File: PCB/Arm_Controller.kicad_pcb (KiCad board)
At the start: 2 copper layers, 156 parts, among them J1 CAN SOCKET, J11 BTN1, J12 FAN1, J15 SWD Header, J2 EXTERNAL POWER, J3 BATTERY POWER, J4 STEP_MOTOR_1, J5 STEP_MOTOR_2, J6 STEP_MOTOR_3, J7 STEP_MOTOR_4, J8 STEP_MOTOR_5, J9 STEP_MOTOR_6, U1 STM32G431CBT6, U10 TMC2209-LA-T, U11 TMC2209-LA-T, U2 XL4005E1, U3 NCP1117-3.3_SOT223, U5 TMC2209-LA-T, U6 ISO1042DWVR, U7 TMC2209-LA-T, U8 TMC2209-LA-T, U9 TMC2209-LA-T, Y1 8MHz

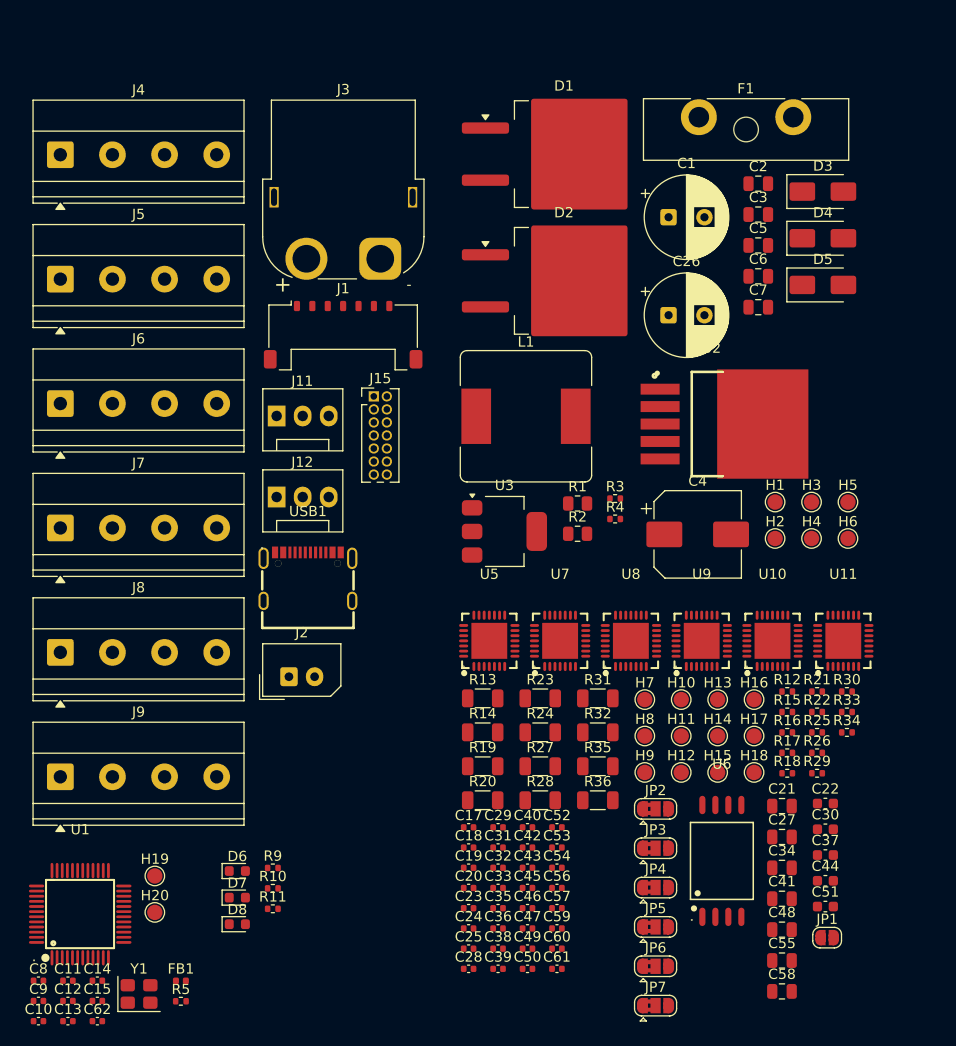
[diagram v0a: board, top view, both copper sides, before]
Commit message: Improved Protection and Board Testability - Added power rail protection and decoupling for stepper motor noise environment - Added TVS, bulk caps and fuse upgrade on 24V rail - Added test pads for bring-up and debugging
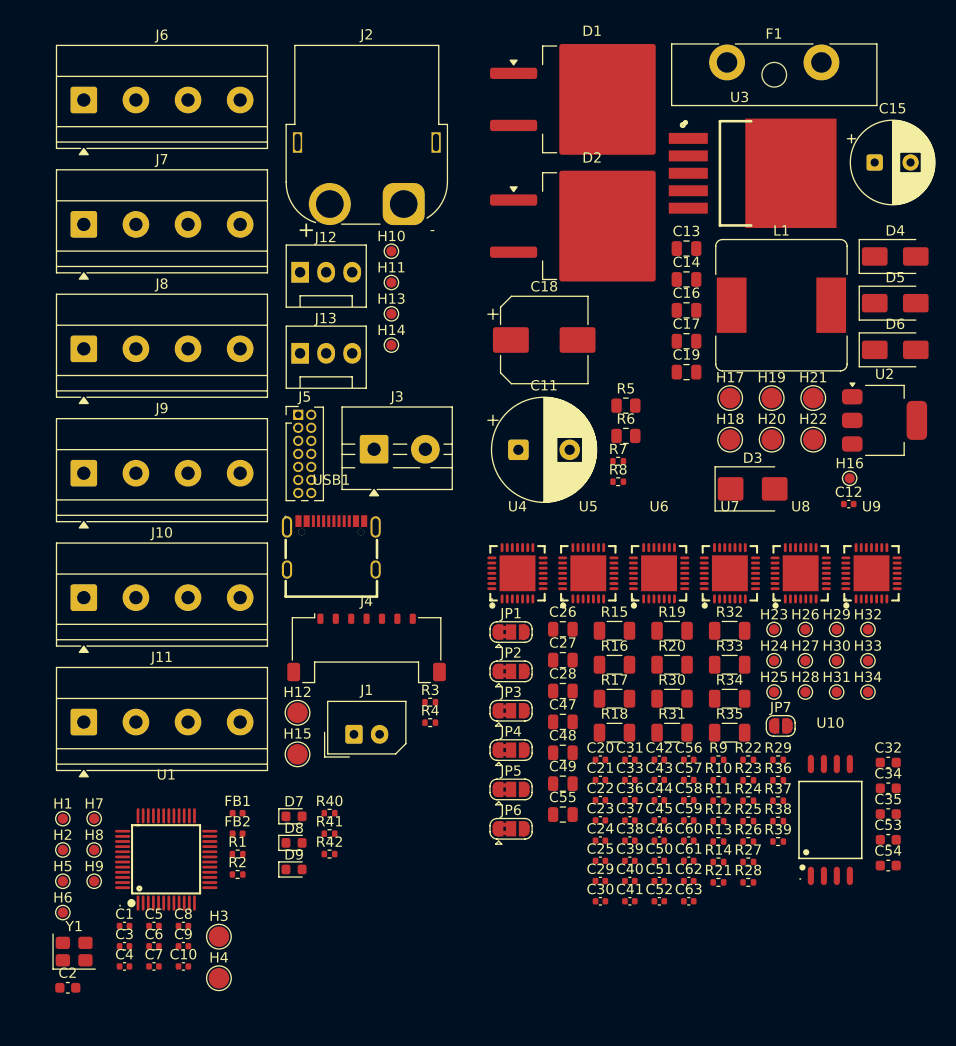
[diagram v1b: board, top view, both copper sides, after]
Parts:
- removed J15: SWD Header, Connector_PinHeader_1.27mm:PinHeader_2x07_P1.27mm_Vertical
- removed U11: TMC2209-LA-T, lcsc:QFN-28_L5.0-W5.0-P0.50-BL-EP
- added C16: 1uF, Capacitor_SMD:C_0805_2012Metric, F.Cu at (139.5, 76.8)
- added C63: 100nF, Capacitor_SMD:C_0402_1005Metric, F.Cu at (139.7, 134.4)
- added D9: LED_GREEN, LED_SMD:LED_0603_1608Metric, F.Cu at (101.3, 131.3)
- added FB2: 1kR@100MHz, Inductor_SMD:L_0402_1005Metric, F.Cu at (95.8, 127.8)
- added H21: +24V, TestPoint:TestPoint_Pad_D2.0mm, F.Cu at (151.9, 85.3)
- added H22: +VBUS, TestPoint:TestPoint_Pad_D2.0mm, F.Cu at (151.9, 89.4)
- added H23: TMC1_DIAG, TestPoint:TestPoint_Pad_D1.0mm, F.Cu at (148.1, 107.9)
- added H24: TMC2_DIAG, TestPoint:TestPoint_Pad_D1.0mm, F.Cu at (148.1, 110.9)
- added H25: TMC3_DIAG, TestPoint:TestPoint_Pad_D1.0mm, F.Cu at (148.1, 114.0)
- added H26: TMC1_INDEX, TestPoint:TestPoint_Pad_D1.0mm, F.Cu at (151.1, 107.9)
- added H27: TMC2_INDEX, TestPoint:TestPoint_Pad_D1.0mm, F.Cu at (151.1, 110.9)
- added H28: TMC3_INDEX, TestPoint:TestPoint_Pad_D1.0mm, F.Cu at (151.1, 114.0)
- added H29: TMC4_DIAG, TestPoint:TestPoint_Pad_D1.0mm, F.Cu at (154.2, 107.9)
- added H30: TMC5_DIAG, TestPoint:TestPoint_Pad_D1.0mm, F.Cu at (154.2, 110.9)
- added H31: TMC6_DIAG, TestPoint:TestPoint_Pad_D1.0mm, F.Cu at (154.2, 114.0)
- added H32: TMC4_INDEX, TestPoint:TestPoint_Pad_D1.0mm, F.Cu at (157.2, 107.9)
- added H33: TMC5_INDEX, TestPoint:TestPoint_Pad_D1.0mm, F.Cu at (157.2, 110.9)
- added H34: TMC6_INDEX, TestPoint:TestPoint_Pad_D1.0mm, F.Cu at (157.2, 114.0)
- added J10: STEP_MOTOR_5, TerminalBlock_Phoenix:TerminalBlock_Phoenix_MKDS-1,5-4-5.08_1x04_P5.08mm_Horizontal, F.Cu at (80.8, 104.8)
- added J13: FAN1, Connector:FanPinHeader_1x03_P2.54mm_Vertical, F.Cu at (101.9, 81.0)
- added R37: 20kR, Resistor_SMD:R_0402_1005Metric, F.Cu at (148.5, 124.6)
- added R38: 20kR, Resistor_SMD:R_0402_1005Metric, F.Cu at (148.5, 126.6)
- added R39: 120R, Resistor_SMD:R_0402_1005Metric, F.Cu at (148.5, 128.6)
- added R40: 1.1kR, Resistor_SMD:R_0402_1005Metric, F.Cu at (104.7, 125.8)
- added R41: 1kR, Resistor_SMD:R_0402_1005Metric, F.Cu at (104.7, 127.8)
- added R42: 390R, Resistor_SMD:R_0402_1005Metric, F.Cu at (104.7, 129.8)
- added R6: 10kR, Resistor_SMD:R_0805_2012Metric, F.Cu at (133.6, 89.0)
- added R7: 5.1kR, Resistor_SMD:R_0402_1005Metric, F.Cu at (132.9, 91.5)
- added R8: 5.1kR, Resistor_SMD:R_0402_1005Metric, F.Cu at (132.9, 93.5)
- added U4: TMC2209-LA-T, lcsc:QFN-28_L5.0-W5.0-P0.50-BL-EP, F.Cu at (123.1, 102.4)
- C1: value 220uF -> 100nF; footprint Capacitor_THT:CP_Radial_D8.0mm_P3.50mm -> Capacitor_SMD:C_0402_1005Metric
- C10: value 100nF -> 10pF
- C11: value 100nF -> 1000uF/50V; footprint Capacitor_SMD:C_0402_1005Metric -> Capacitor_THT:CP_Radial_D10.0mm_P5.00mm
- C12, C29, C36, C50, C57: value 100nF -> 100nF/50V
- C13: value 10nF -> 10uF; footprint Capacitor_SMD:C_0402_1005Metric -> Capacitor_SMD:C_0805_2012Metric
- C14: value 1uF -> 10uF; footprint Capacitor_SMD:C_0402_1005Metric -> Capacitor_SMD:C_0805_2012Metric
- C15: value 1uF -> 220uF; footprint Capacitor_SMD:C_0402_1005Metric -> Capacitor_THT:CP_Radial_D8.0mm_P3.50mm
- C17: value 100nF -> 1uF; footprint Capacitor_SMD:C_0402_1005Metric -> Capacitor_SMD:C_0805_2012Metric
- C18: value 100nF -> 330uF; footprint Capacitor_SMD:C_0402_1005Metric -> Capacitor_SMD:CP_Elec_8x10
- C19: value 22nF -> 10nF; footprint Capacitor_SMD:C_0402_1005Metric -> Capacitor_SMD:C_0805_2012Metric
- C2: value 1uF -> 47uF; footprint Capacitor_SMD:C_0805_2012Metric -> Capacitor_SMD:C_0603_1608Metric
- C20, C43: value 100nF -> 22nF
- C21, C41: value 4.7uF -> 22nF; footprint Capacitor_SMD:C_0805_2012Metric -> Capacitor_SMD:C_0402_1005Metric
- C22: value 1uF/50V -> 22nF; footprint Capacitor_SMD:C_0603_1608Metric -> Capacitor_SMD:C_0402_1005Metric
- C23, C24, C25, C45, C46: value 100nF/50V -> 100nF
- C26: value 47uF/50V -> 4.7uF; footprint Capacitor_THT:CP_Radial_D8.0mm_P3.50mm -> Capacitor_SMD:C_0805_2012Metric
- C28, C49: value 22nF -> 4.7uF; footprint Capacitor_SMD:C_0402_1005Metric -> Capacitor_SMD:C_0805_2012Metric
- C3: value 1uF -> 100nF; footprint Capacitor_SMD:C_0805_2012Metric -> Capacitor_SMD:C_0402_1005Metric
- C30, C37, C51: value 1uF/50V -> 100nF/50V; footprint Capacitor_SMD:C_0603_1608Metric -> Capacitor_SMD:C_0402_1005Metric
- C32, C53, C54: value 100nF/50V -> 1uF/50V; footprint Capacitor_SMD:C_0402_1005Metric -> Capacitor_SMD:C_0603_1608Metric
- C34: value 4.7uF -> 1uF/50V; footprint Capacitor_SMD:C_0805_2012Metric -> Capacitor_SMD:C_0603_1608Metric
- C35: value 22nF -> 1uF/50V; footprint Capacitor_SMD:C_0402_1005Metric -> Capacitor_SMD:C_0603_1608Metric
- C4: value 330uF -> 100nF; footprint Capacitor_SMD:CP_Elec_8x10 -> Capacitor_SMD:C_0402_1005Metric
- C44: value 1uF/50V -> 100nF; footprint Capacitor_SMD:C_0603_1608Metric -> Capacitor_SMD:C_0402_1005Metric
- C47: value 100nF/50V -> 4.7uF; footprint Capacitor_SMD:C_0402_1005Metric -> Capacitor_SMD:C_0805_2012Metric
- C5: value 10nF -> 100nF; footprint Capacitor_SMD:C_0805_2012Metric -> Capacitor_SMD:C_0402_1005Metric
- C55: value 4.7uF -> 1uF/50V
- C56: value 22nF -> 100nF/50V
- C58: value 1uF/50V -> 100nF/50V; footprint Capacitor_SMD:C_0805_2012Metric -> Capacitor_SMD:C_0402_1005Metric
- C6: value 10uF -> 100nF; footprint Capacitor_SMD:C_0805_2012Metric -> Capacitor_SMD:C_0402_1005Metric
- C7: value 10uF -> 1uF; footprint Capacitor_SMD:C_0805_2012Metric -> Capacitor_SMD:C_0402_1005Metric
- C8: value 10pF -> 100nF
- D3: value SS14 -> SMBJ26A; footprint Diode_SMD:D_SMA -> Diode_SMD:D_SMB
- D4: value SS56 -> SS14
- D6: value LED_RED -> SS56; footprint LED_SMD:LED_0603_1608Metric -> Diode_SMD:D_SMA
- D8: value LED_GREEN -> LED_RED
- F1: value 15A/32V -> 15A/50V
- FB1: value 1kR@100MHz -> 600R@100MHz
- H1: value GND -> BOOT; footprint TestPoint:TestPoint_Pad_D1.5mm -> TestPoint:TestPoint_Pad_D1.0mm
- H10: value TMC2_INDEX -> SWDIO; footprint TestPoint:TestPoint_Pad_D1.5mm -> TestPoint:TestPoint_Pad_D1.0mm
- H11: value TMC3_DIAG -> SWCLK; footprint TestPoint:TestPoint_Pad_D1.5mm -> TestPoint:TestPoint_Pad_D1.0mm
- H12: value TMC3_INDEX -> CAN_VCC; footprint TestPoint:TestPoint_Pad_D1.5mm -> TestPoint:TestPoint_Pad_D2.0mm
- H13: value TMC4_DIAG -> CAN_H; footprint TestPoint:TestPoint_Pad_D1.5mm -> TestPoint:TestPoint_Pad_D1.0mm
- H14: value TMC4_INDEX -> CAN_L; footprint TestPoint:TestPoint_Pad_D1.5mm -> TestPoint:TestPoint_Pad_D1.0mm
- H15: value TMC5_DIAG -> CAN_GND; footprint TestPoint:TestPoint_Pad_D1.5mm -> TestPoint:TestPoint_Pad_D2.0mm
- H16: value TMC5_INDEX -> SW; footprint TestPoint:TestPoint_Pad_D1.5mm -> TestPoint:TestPoint_Pad_D1.0mm
- H17: value TMC6_DIAG -> CC2; footprint TestPoint:TestPoint_Pad_D1.5mm -> TestPoint:TestPoint_Pad_D2.0mm
- H18: value TMC6_INDEX -> CC1; footprint TestPoint:TestPoint_Pad_D1.5mm -> TestPoint:TestPoint_Pad_D2.0mm
- H19: value BOOT -> GND; footprint TestPoint:TestPoint_Pad_D1.5mm -> TestPoint:TestPoint_Pad_D2.0mm
- H2: value 3V3 -> NRST; footprint TestPoint:TestPoint_Pad_D1.5mm -> TestPoint:TestPoint_Pad_D1.0mm
- H20: value SPARE_GPIO -> +3V3; footprint TestPoint:TestPoint_Pad_D1.5mm -> TestPoint:TestPoint_Pad_D2.0mm
- H3: value 24V -> VDDA; footprint TestPoint:TestPoint_Pad_D1.5mm -> TestPoint:TestPoint_Pad_D2.0mm
- H4: value VBUS -> VREF+; footprint TestPoint:TestPoint_Pad_D1.5mm -> TestPoint:TestPoint_Pad_D2.0mm
- H5: value CC2 -> SPARE_GPIO; footprint TestPoint:TestPoint_Pad_D1.5mm -> TestPoint:TestPoint_Pad_D1.0mm
- H6: value CC1 -> CAN_RX; footprint TestPoint:TestPoint_Pad_D1.5mm -> TestPoint:TestPoint_Pad_D1.0mm
- H7: value TMC1_DIAG -> USART2; footprint TestPoint:TestPoint_Pad_D1.5mm -> TestPoint:TestPoint_Pad_D1.0mm
- H8: value TMC1_INDEX -> CAN_TX; footprint TestPoint:TestPoint_Pad_D1.5mm -> TestPoint:TestPoint_Pad_D1.0mm
- H9: value TMC2_DIAG -> USART1; footprint TestPoint:TestPoint_Pad_D1.5mm -> TestPoint:TestPoint_Pad_D1.0mm
- J1: value CAN SOCKET -> EXTN_PWR; footprint Connector_Molex:Molex_Pico-Lock_504050-0791_1x07-1MP_P1.50mm_Horizontal -> Connector_Molex:Molex_SPOX_5267-02A_1x02_P2.50mm_Vertical
- J11: value BTN1 -> STEP_MOTOR_6; footprint Connector:FanPinHeader_1x03_P2.54mm_Vertical -> TerminalBlock_Phoenix:TerminalBlock_Phoenix_MKDS-1,5-4-5.08_1x04_P5.08mm_Horizontal
- J12: value FAN1 -> BTN1
- J2: value EXTERNAL POWER -> PWR_BATT; footprint Connector_Molex:Molex_SPOX_5267-02A_1x02_P2.50mm_Vertical -> Connector_AMASS:AMASS_XT60PW-F_1x02_P7.20mm_Horizontal
- J3: value BATTERY POWER -> PWR_24V; footprint Connector_AMASS:AMASS_XT60PW-F_1x02_P7.20mm_Horizontal -> TerminalBlock:TerminalBlock_MaiXu_MX126-5.0-02P_1x02_P5.00mm
- J4: value STEP_MOTOR_1 -> CAN SOCKET; footprint TerminalBlock_Phoenix:TerminalBlock_Phoenix_MKDS-1,5-4-5.08_1x04_P5.08mm_Horizontal -> Connector_Molex:Molex_Pico-Lock_504050-0791_1x07-1MP_P1.50mm_Horizontal
- J5: value STEP_MOTOR_2 -> SWD Header; footprint TerminalBlock_Phoenix:TerminalBlock_Phoenix_MKDS-1,5-4-5.08_1x04_P5.08mm_Horizontal -> Connector_PinHeader_1.27mm:PinHeader_2x07_P1.27mm_Vertical
- J6: value STEP_MOTOR_3 -> STEP_MOTOR_1
- J7: value STEP_MOTOR_4 -> STEP_MOTOR_2
- J8: value STEP_MOTOR_5 -> STEP_MOTOR_3
- J9: value STEP_MOTOR_6 -> STEP_MOTOR_4
- JP1: value CAN TERM -> TMC1_SPREAD; footprint Jumper:SolderJumper-2_P1.3mm_Open_RoundedPad1.0x1.5mm -> Jumper:SolderJumper-3_P1.3mm_Bridged2Bar12_RoundedPad1.0x1.5mm
- JP2: value TMC1_SPREAD -> TMC2_SPREAD
- JP3: value TMC2_SPREAD -> TMC3_SPREAD
- JP4: value TMC3_SPREAD -> TMC4_SPREAD
- JP5: value TMC4_SPREAD -> TMC5_SPREAD
- JP6: value TMC5_SPREAD -> TMC6_SPREAD
- JP7: value TMC6_SPREAD -> CAN TERM; footprint Jumper:SolderJumper-3_P1.3mm_Bridged2Bar12_RoundedPad1.0x1.5mm -> Jumper:SolderJumper-2_P1.3mm_Open_RoundedPad1.0x1.5mm
- R1: value 10kR -> 0R; footprint Resistor_SMD:R_0805_2012Metric -> Resistor_SMD:R_0402_1005Metric
- R10: value 1.1kR -> 100R
- R11: value 390R -> 100R
- R12: value 120R -> 20kR
- R13, R14, R23, R27, R28, R36: value 0R11 -> 20kR; footprint Resistor_SMD:R_1206_3216Metric -> Resistor_SMD:R_0402_1005Metric
- R15, R16, R17, R18, R30, R33, R34: value 20kR -> 0R11; footprint Resistor_SMD:R_0402_1005Metric -> Resistor_SMD:R_1206_3216Metric
- R2: value 33kR -> 10kR; footprint Resistor_SMD:R_0805_2012Metric -> Resistor_SMD:R_0402_1005Metric
- R24: value 0R11 -> 100R; footprint Resistor_SMD:R_1206_3216Metric -> Resistor_SMD:R_0402_1005Metric
- R25, R26: value 20kR -> 100R
- R3, R4: value 5.1kR -> 10kR
- R5: value 0R -> 33kR; footprint Resistor_SMD:R_0402_1005Metric -> Resistor_SMD:R_0805_2012Metric
- R9: value 1kR -> 100R
- U10: value TMC2209-LA-T -> ISO1042DWVR; footprint lcsc:QFN-28_L5.0-W5.0-P0.50-BL-EP -> lcsc:SOIC-8_L7.5-W5.9-P1.27-LS11.5-BL
- U2: value XL4005E1 -> NCP1117-3.3_SOT223; footprint lcsc:TO-263-5_L10.2-W9.2-P1.70-TL -> Package_TO_SOT_SMD:SOT-223-3_TabPin2
- U3: value NCP1117-3.3_SOT223 -> XL4005E1; footprint Package_TO_SOT_SMD:SOT-223-3_TabPin2 -> lcsc:TO-263-5_L10.2-W9.2-P1.70-TL
- U6: value ISO1042DWVR -> TMC2209-LA-T; footprint lcsc:SOIC-8_L7.5-W5.9-P1.27-LS11.5-BL -> lcsc:QFN-28_L5.0-W5.0-P0.50-BL-EP
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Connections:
- C1 pad 1: +24V -> +3V3
- C10 pad 1: +3.3V -> OSC_IN
- C10 pad 2: Net-(C10-Pad2) -> GND
- C11 pad 1: +3.3V -> +24V
- C11 pad 2: Net-(C10-Pad2) -> GND
- C12 pad 1: +3.3V -> +24V
- C12 pad 2: Net-(C10-Pad2) -> GND
- C13 pad 1: VDD33A -> VBUS
- C13 pad 2: Net-(C10-Pad2) -> GND
- C14 pad 1: Net-(C14-Pad1) -> Net-(D5-A)
- C14 pad 2: Net-(C10-Pad2) -> GND
- C15 pad 1: VREF+ -> +24V
- C15 pad 2: Net-(C10-Pad2) -> GND
- C17 pad 1: +3V3 -> Net-(D4-A)
- C18 pad 1: CAN_VCC -> Net-(D4-A)
- C18 pad 2: CAN_GND -> GND
- C19 pad 1: Net-(U5-CPI) -> Net-(D4-A)
- C19 pad 2: Net-(U5-CPO) -> Net-(U3-FB)
- C2 pad 1: +24V -> Net-(C2-Pad1)
- C2 pad 2: GND -> Net-(C2-Pad2)
- C20 pad 1: +24V -> Net-(U4-CPI)
- C20 pad 2: Net-(U5-VCP) -> Net-(U4-CPO)
- C21 pad 1: GND -> Net-(U5-CPI)
- C21 pad 2: Net-(U5-5VOUT) -> Net-(U5-CPO)
- C22 pad 1: +24V -> Net-(U6-CPI)
- C22 pad 2: GND -> Net-(U6-CPO)
- C23 pad 2: GND -> Net-(U4-VCP)
- C24 pad 2: GND -> Net-(U5-VCP)
- C25 pad 1: +3V3 -> +24V
- C25 pad 2: GND -> Net-(U6-VCP)
- C26 pad 1: +24V -> GND
- C26 pad 2: GND -> Net-(U4-5VOUT)
- C27 pad 2: Net-(U7-5VOUT) -> Net-(U5-5VOUT)
- C28 pad 1: Net-(U7-CPI) -> GND
- C28 pad 2: Net-(U7-CPO) -> Net-(U6-5VOUT)
- C29 pad 1: +24V -> +3V3
- C29 pad 2: Net-(U7-VCP) -> GND
- C3 pad 1: Net-(D3-A) -> Net-(C2-Pad1)
- C3 pad 2: GND -> Net-(C2-Pad2)
- C30 pad 1: +24V -> +3V3
- C31 pad 1: +24V -> +3V3
- C33 pad 1: +3V3 -> +24V
- C34 pad 1: GND -> +24V
- C34 pad 2: Net-(U8-5VOUT) -> GND
- C35 pad 1: Net-(U8-CPI) -> +24V
- C35 pad 2: Net-(U8-CPO) -> GND
- C36 pad 2: Net-(U8-VCP) -> GND
- C4 pad 1: Net-(D3-A) -> Net-(C2-Pad1)
- C4 pad 2: GND -> Net-(C2-Pad2)
- C40 pad 1: +3V3 -> +24V
- C41 pad 1: GND -> Net-(U7-CPI)
- C41 pad 2: Net-(U9-5VOUT) -> Net-(U7-CPO)
- C42 pad 1: Net-(U9-CPI) -> Net-(U8-CPI)
- C42 pad 2: Net-(U9-CPO) -> Net-(U8-CPO)
- C43 pad 1: +24V -> Net-(U9-CPI)
- C43 pad 2: Net-(U9-VCP) -> Net-(U9-CPO)
- C44 pad 2: GND -> Net-(U7-VCP)
- C45 pad 2: GND -> Net-(U8-VCP)
- C46 pad 2: GND -> Net-(U9-VCP)
- C47 pad 1: +3V3 -> GND
- C47 pad 2: GND -> Net-(U7-5VOUT)
- C48 pad 2: Net-(U10-5VOUT) -> Net-(U8-5VOUT)
- C49 pad 1: Net-(U10-CPI) -> GND
- C49 pad 2: Net-(U10-CPO) -> Net-(U9-5VOUT)
- C5 pad 1: Net-(D3-A) -> Net-(C2-Pad1)
- C5 pad 2: Net-(U2-FB) -> Net-(C2-Pad2)
- C50 pad 1: +24V -> +3V3
- C50 pad 2: Net-(U10-VCP) -> GND
- C51 pad 1: +24V -> +3V3
- C52 pad 1: +24V -> +3V3
- C54 pad 1: +3V3 -> +24V
- C55 pad 1: GND -> +24V
- C55 pad 2: Net-(U11-5VOUT) -> GND
- C56 pad 1: Net-(U11-CPI) -> +24V
- C56 pad 2: Net-(U11-CPO) -> GND
- C57 pad 2: Net-(U11-VCP) -> GND
- C6 pad 1: VBUS -> VDD33A
- C6 pad 2: GND -> Net-(C2-Pad2)
- C61 pad 1: +3V3 -> +24V
- C7 pad 1: Net-(D5-A) -> Net-(C7-Pad1)
- C7 pad 2: GND -> Net-(C2-Pad2)
- C8 pad 1: GND -> VREF+
- C8 pad 2: OSC_OUT -> Net-(C2-Pad2)
- C9 pad 1: OSC_IN -> GND
- C9 pad 2: GND -> OSC_OUT
- D1 pad 2: VBAT -> VDC
- D2 pad 2: VDC -> VBAT
- D3 pad 1: +3.3V -> +24V
- D3 pad 2: Net-(D3-A) -> GND
- D4 pad 1: Net-(D4-K) -> +3.3V
- D4 pad 2: GND -> Net-(D4-A)
- D6 pad 1: GND -> Net-(D6-K)
- D6 pad 2: Net-(D6-A) -> GND
- FB1 pad 2: Net-(C14-Pad1) -> Net-(C2-Pad1)
- H1 pad 1: GND -> CAN_RX
- H10 pad 1: Net-(U7-INDEX) -> SWDIO
- H11 pad 1: TMC3_DIAG -> SWCLK
- H12 pad 1: Net-(U8-INDEX) -> CAN_VCC
- H13 pad 1: TMC4_DIAG -> CAN_H
- H14 pad 1: Net-(U9-INDEX) -> CAN_L
- H15 pad 1: TMC5_DIAG -> CAN_GND
- H16 pad 1: Net-(U10-INDEX) -> Net-(D6-K)
- H17 pad 1: TMC6_DIAG -> CC2
- H18 pad 1: Net-(U11-INDEX) -> CC1
- H19 pad 1: CAN_RX -> GND
- H2 pad 1: +3.3V -> NRST
- H20 pad 1: Net-(U1-PA2) -> +3.3V
- H3 pad 1: +24V -> VDD33A
- H4 pad 1: VBUS -> VREF+
- H5 pad 1: CC2 -> Net-(U1-PA2)
- H6 pad 1: CC1 -> CAN_RX
- H7 pad 1: TMC1_DIAG -> USART2
- H8 pad 1: Net-(U5-INDEX) -> CAN_TX
- H9 pad 1: TMC2_DIAG -> USART1
- J1 pad 1: unconnected-(J1-Pin_1-Pad1) -> VDC
- J1 pad 2: unconnected-(J1-Pin_2-Pad2) -> GND
- J11 pad 1: +3V3 -> TMC6_A1
- J11 pad 2: GPIO_EXTRN1 -> TMC6_A2
- J11 pad 3: GND -> TMC6_B1
- J12 pad 2: GPIO_EXTRN2 -> GPIO_EXTRN1
- J2 pad 1: VDC -> VBAT
- J3 pad 1: VBAT -> +24V
- J4 pad 1: TMC1_A1 -> unconnected-(J4-Pin_1-Pad1)
- J4 pad 2: TMC1_A2 -> unconnected-(J4-Pin_2-Pad2)
- J4 pad 3: TMC1_B1 -> unconnected-(J4-Pin_3-Pad3)
- J4 pad 4: TMC1_B2 -> unconnected-(J4-Pin_4-Pad4)
- J5 pad 1: TMC2_A1 -> unconnected-(J5-Pin_1-Pad1)
- J5 pad 2: TMC2_A2 -> unconnected-(J5-Pin_2-Pad2)
- J5 pad 3: TMC2_B1 -> +3V3
- J5 pad 4: TMC2_B2 -> SWDIO
- J6 pad 1: TMC3_A1 -> TMC1_A1
- J6 pad 2: TMC3_A2 -> TMC1_A2
- J6 pad 3: TMC3_B1 -> TMC1_B1
- J6 pad 4: TMC3_B2 -> TMC1_B2
- J7 pad 1: TMC4_A1 -> TMC2_A1
- J7 pad 2: TMC4_A2 -> TMC2_A2
- J7 pad 3: TMC4_B1 -> TMC2_B1
- J7 pad 4: TMC4_B2 -> TMC2_B2
- J8 pad 1: TMC5_A1 -> TMC3_A1
- J8 pad 2: TMC5_A2 -> TMC3_A2
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
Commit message: PCB Layout: Initial TMC2209 driver cluster layout
- Defined netclasses for 24V, Stepper Motor, 3V3, 5V and Signal
- Decided on 4-layer stackup: Signal / GND / Power / Signal
- Routed high current motor output traces with tapered zone fills
- Placed and routed VS decoupling caps (100nF, 1uF, 47uF electrolytic)
- Routed sense resistors with dedicated GND vias per resistor
- Routed BRA/BRB via bottom layer with perpendicular crossing under motor traces
- Planned +24V / +3V3 split power plane on L3
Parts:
- added C64: 100nF/50V, Capacitor_SMD:C_0402_1005Metric, F.Cu at (-714.8, 53.8)
- added C65: 47uF/50V, Capacitor_SMD:CP_Elec_8x10.5, F.Cu at (-185.1, -10.7)
- added C66: 47uF/50V, Capacitor_SMD:CP_Elec_8x10.5, F.Cu at (-707.2, -89.6)
- added C67: 47uF/50V, Capacitor_SMD:CP_Elec_8x10.5, F.Cu at (-724.9, 63.2)
- added C68: 100nF, Capacitor_SMD:C_0402_1005Metric, F.Cu at (393.6, 115.5)
- added C69: 100nF, Capacitor_SMD:C_0402_1005Metric, F.Cu at (355.1, 187.8)
- C33, C56, C57: value 100nF/50V -> 1uF/50V; footprint Capacitor_SMD:C_0402_1005Metric -> Capacitor_SMD:C_0603_1608Metric
- C35, C53, C54: value 1uF/50V -> 100nF/50V; footprint Capacitor_SMD:C_0603_1608Metric -> Capacitor_SMD:C_0402_1005Metric
- C41, C42, C43: value 22nF -> 47uF/50V; footprint Capacitor_SMD:C_0402_1005Metric -> Capacitor_SMD:CP_Elec_8x10.5
- C44, C45, C46: value 100nF -> 22nF
- C47, C48, C49: value 4.7uF -> 100nF; footprint Capacitor_SMD:C_0805_2012Metric -> Capacitor_SMD:C_0402_1005Metric
- C50, C51, C52: value 100nF/50V -> 4.7uF; footprint Capacitor_SMD:C_0402_1005Metric -> Capacitor_SMD:C_0805_2012Metric
- C55: value 1uF/50V -> 100nF/50V; footprint Capacitor_SMD:C_0805_2012Metric -> Capacitor_SMD:C_0402_1005Metric
- C58: value 100nF/50V -> 1uF/50V; footprint Capacitor_SMD:C_0402_1005Metric -> Capacitor_SMD:C_0805_2012Metric
- C62, C63: value 100nF -> 100nF/50V
- D9: value LED_GREEN -> LED_BLUE
- moved C45 891.5 mm to (-729.5, -83.4)
- moved C48 891.5 mm to (-738.9, -89.9)
- moved C51 891.5 mm to (-729.5, -77.4)
- moved C57 891.5 mm to (-726.7, -87.3)
- moved C60 891.5 mm to (-726.7, -81.4)
- moved H30 891.5 mm to (-712.3, -98.9)
- moved R31 891.5 mm to (-728.3, -91.9)
- moved R34 891.5 mm to (-722.7, -95.2)
- moved U8 891.5 mm to (-715.8, -107.4)
- moved C54 891.5 mm to (-707.2, -79.0)
- moved H33 891.5 mm to (-709.2, -98.9)
- moved JP5 891.5 mm to (-744.0, -86.4)
- moved R25 891.5 mm to (-720.9, -83.3)
- moved R28 891.5 mm to (-720.9, -77.3)
- moved R37 891.5 mm to (-718.0, -85.3)
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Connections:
- C41 pad 1: Net-(U7-CPI) -> +24V
- C41 pad 2: Net-(U7-CPO) -> GND
- C42 pad 1: Net-(U8-CPI) -> +24V
- C42 pad 2: Net-(U8-CPO) -> GND
- C43 pad 1: Net-(U9-CPI) -> +24V
- C43 pad 2: Net-(U9-CPO) -> GND
- C44 pad 1: +24V -> Net-(U7-CPI)
- C44 pad 2: Net-(U7-VCP) -> Net-(U7-CPO)
- C45 pad 1: +24V -> Net-(U8-CPI)
- C45 pad 2: Net-(U8-VCP) -> Net-(U8-CPO)
- C46 pad 1: +24V -> Net-(U9-CPI)
- C46 pad 2: Net-(U9-VCP) -> Net-(U9-CPO)
- C47 pad 1: GND -> +24V
- C47 pad 2: Net-(U7-5VOUT) -> Net-(U7-VCP)
- C48 pad 1: GND -> +24V
- C48 pad 2: Net-(U8-5VOUT) -> Net-(U8-VCP)
- C49 pad 1: GND -> +24V
- C49 pad 2: Net-(U9-5VOUT) -> Net-(U9-VCP)
- C50 pad 1: +3V3 -> GND
- C50 pad 2: GND -> Net-(U7-5VOUT)
- C51 pad 1: +3V3 -> GND
- C51 pad 2: GND -> Net-(U8-5VOUT)
- C52 pad 1: +3V3 -> GND
- C52 pad 2: GND -> Net-(U9-5VOUT)
- C53 pad 1: +24V -> +3V3
- C54 pad 1: +24V -> +3V3
- C55 pad 1: +24V -> +3V3
- C62 pad 1: +3V3 -> +24V
- C63 pad 1: CAN_VCC -> +24V
- C63 pad 2: CAN_GND -> GND
- J10 pad 1: TMC5_A1 -> TMC5_A2
- J10 pad 2: TMC5_A2 -> TMC5_A1
- J11 pad 1: TMC6_A1 -> TMC6_A2
- J11 pad 2: TMC6_A2 -> TMC6_A1
- J6 pad 1: TMC1_A1 -> TMC1_A2
- J6 pad 2: TMC1_A2 -> TMC1_A1
- J7 pad 1: TMC2_A1 -> TMC2_A2
- J7 pad 2: TMC2_A2 -> TMC2_A1
- J8 pad 1: TMC3_A1 -> TMC3_A2
- J8 pad 2: TMC3_A2 -> TMC3_A1
- J9 pad 1: TMC4_A1 -> TMC4_A2
- J9 pad 2: TMC4_A2 -> TMC4_A1
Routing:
- net TMC4_A2: track 0.00 -> 20.1 mm
- net TMC4_B2: track 0.00 -> 17.4 mm
- net TMC4_A1: track 0.00 -> 15.8 mm
- net TMC4_B1: track 0.00 -> 15.7 mm
- net GND: track 0.00 -> 15.0 mm, vias 0 -> 8
- net Net-(U7-BRB): track 0.00 -> 11.7 mm, vias 0 -> 2
- net +24V: track 0.00 -> 8.86 mm, vias 0 -> 3
- net Net-(U7-BRA): track 0.00 -> 8.81 mm, vias 0 -> 2
- net TMC_B_ENN: track 0.00 -> 7.03 mm
- net Net-(U7-INDEX): track 0.00 -> 5.71 mm
- net TMC4_SPREAD: track 0.00 -> 5.01 mm
- net +3V3: track 0.00 -> 4.56 mm, vias 0 -> 3
- net Net-(U7-VCP): track 0.00 -> 4.01 mm
- net TMC4_DIAG: track 0.00 -> 3.67 mm
- net Net-(U7-CPI): track 0.00 -> 2.65 mm
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- added copper zone on F.Cu, net +24V
- added copper zone on F.Cu, net GND
- added copper zone on F.Cu, net Net-(U7-5VOUT)
- added copper zone on F.Cu, net TMC4_A1
- added copper zone on F.Cu, net TMC4_A2
- added copper zone on F.Cu, net TMC4_B1
- added copper zone on F.Cu, net TMC4_B2
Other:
- copper layers 2 -> 4

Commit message: Started laying out the PCB - Decided for a square-shaped board - Split Motor Controllers on top and bottom - Split Power Plane (+3V3 on logic side, +24V on motor side) - Roughly layed out the board entirely - Reconsidered my life choises (got sick)
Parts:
- removed the C22 at (-586.4, 57.4)
- removed the C23 at (-575.1, -211.4)
- removed the C24 at (-577.7, -85.0)
- removed the C25 at (-586.4, 63.3)
- removed the C26 at (-578.8, -230.0)
- removed the C27 at (-581.3, -102.5)
- removed the C28 at (-590.1, 46.8)
- removed the C29 at (-575.1, -205.5)
- removed the H23 at (-558.2, -230.0)
- removed the H24 at (-560.7, -102.5)
- removed the JP2 at (-586.4, -101.5)
- removed the R13 at (-566.2, -84.9)
- removed the R14 at (-574.9, 63.4)
- removed the R15 at (-573.7, -229.9)
- removed the R16 at (-576.3, -102.1)
- removed the R17 at (-585.0, 47.5)
- removed the U5 at (-578.8, -111.0)
- added C44: 47uF/50V, Capacitor_SMD:CP_Elec_8x10.5, F.Cu at (91.3, 121.7)
- added C47: 22nF, Capacitor_SMD:C_0402_1005Metric, F.Cu at (94.2, 71.1)
- added C50: 100nF/50V, Capacitor_SMD:C_0402_1005Metric, F.Cu at (96.3, 65.5)
- added C53: 100nF/50V, Capacitor_SMD:C_0402_1005Metric, F.Cu at (102.5, 71.6)
- added C56: 100nF, Capacitor_SMD:C_0402_1005Metric, F.Cu at (114.1, 72.2)
- added C59: 100nF/50V, Capacitor_SMD:C_0402_1005Metric, F.Cu at (121.9, 65.4)
- added C62: 4.7uF, Capacitor_SMD:C_0805_2012Metric, F.Cu at (139.6, 74.4)
- added C65: 1uF/50V, Capacitor_SMD:C_0603_1608Metric, F.Cu at (138.0, 63.9)
- added C70: 100nF/50V, Capacitor_SMD:C_0603_1608Metric, F.Cu at (156.8, 130.2)
- added D10: SMBJ26A, Diode_SMD:D_SMB, F.Cu at (153.7, 130.2)
- added H29: TMC4_DIAG, TestPoint:TestPoint_Pad_D1.0mm, F.Cu at (98.8, 75.5)
- added H32: TMC4_INDEX, TestPoint:TestPoint_Pad_D1.0mm, F.Cu at (121.9, 77.1)
- added H35: +24V, TestPoint:TestPoint_Pad_D2.0mm, F.Cu at (102.0, 82.3)
- added H36: GND, TestPoint:TestPoint_Pad_D2.0mm, F.Cu at (102.0, 86.4)
- added H37: +24V, TestPoint:TestPoint_Pad_D2.0mm, F.Cu at (106.0, 82.3)
- added H38: +24V, TestPoint:TestPoint_Pad_D2.0mm, F.Cu at (106.0, 86.4)
- added H39: GND, TestPoint:TestPoint_Pad_D2.0mm, F.Cu at (110.1, 82.3)
- added H40: GND, TestPoint:TestPoint_Pad_D2.0mm, F.Cu at (110.1, 86.4)
- added JP4: TMC4_SPREAD, Jumper:SolderJumper-3_P1.3mm_Bridged2Bar12_RoundedPad1.0x1.5mm, F.Cu at (102.9, 107.8)
- added R24: 20kR, Resistor_SMD:R_0402_1005Metric, F.Cu at (96.0, 109.8)
- added R27: 0R11, Resistor_SMD:R_1206_3216Metric, F.Cu at (94.6, 114.9)
- added R30: 20kR, Resistor_SMD:R_0402_1005Metric, F.Cu at (91.8, 70.5)
- added R33: 100R, Resistor_SMD:R_0402_1005Metric, F.Cu at (114.0, 74.2)
- added R36: 0R11, Resistor_SMD:R_1206_3216Metric, F.Cu at (115.6, 67.6)
- added U7: TMC2209-LA-T, lcsc:QFN-28_L5.0-W5.0-P0.50-BL-EP, F.Cu at (98.8, 113.3)
- C10: value 10pF -> 100nF
- C11: value 1000uF/50V -> 220uF; footprint Capacitor_THT:CP_Radial_D10.0mm_P5.00mm -> Capacitor_THT:CP_Radial_D8.0mm_P3.50mm
- C12: value 100nF/50V -> 1uF; footprint Capacitor_SMD:C_0402_1005Metric -> Capacitor_SMD:C_0805_2012Metric
- C13: value 10uF -> 1000uF/50V; footprint Capacitor_SMD:C_0805_2012Metric -> Capacitor_THT:CP_Radial_D10.0mm_P5.00mm
- C14: value 10uF -> 1uF
- C15: value 220uF -> 100nF/50V; footprint Capacitor_THT:CP_Radial_D8.0mm_P3.50mm -> Capacitor_SMD:C_0603_1608Metric
- C16: value 1uF -> 330uF; footprint Capacitor_SMD:C_0805_2012Metric -> Capacitor_SMD:CP_Elec_8x10
- C17: value 1uF -> 10nF
- C18: value 330uF -> 10uF; footprint Capacitor_SMD:CP_Elec_8x10 -> Capacitor_SMD:C_0805_2012Metric
- C19: value 10nF -> 10uF
- C2: value 47uF -> 10pF; footprint Capacitor_SMD:C_0603_1608Metric -> Capacitor_SMD:C_0402_1005Metric
- C20, C21: value 22nF -> 100nF
- C22: renamed from C44; value 22nF -> 4.7uF; footprint Capacitor_SMD:C_0402_1005Metric -> Capacitor_SMD:C_0805_2012Metric
- C23: renamed from C47; value 100nF -> 22nF
- C24: renamed from C50; value 4.7uF -> 100nF; footprint Capacitor_SMD:C_0805_2012Metric -> Capacitor_SMD:C_0402_1005Metric
- C25: renamed from C53; value 100nF/50V -> 1uF/50V; footprint Capacitor_SMD:C_0402_1005Metric -> Capacitor_SMD:C_0603_1608Metric
- C26: renamed from C56; value 1uF/50V -> 100nF/50V; footprint Capacitor_SMD:C_0603_1608Metric -> Capacitor_SMD:C_0402_1005Metric
- C28: renamed from C62; value 100nF/50V -> 47uF/50V; footprint Capacitor_SMD:C_0402_1005Metric -> Capacitor_SMD:CP_Elec_8x10.5
- C29: renamed from C65; value 47uF/50V -> 100nF/50V; footprint Capacitor_SMD:CP_Elec_8x10.5 -> Capacitor_SMD:C_0402_1005Metric
- C3: value 100nF -> 10pF
- C30, C38, C54: value 100nF/50V -> 4.7uF; footprint Capacitor_SMD:C_0402_1005Metric -> Capacitor_SMD:C_0805_2012Metric
- C31, C39, C55, C63: value 100nF/50V -> 22nF
- C32: value 1uF/50V -> 100nF; footprint Capacitor_SMD:C_0603_1608Metric -> Capacitor_SMD:C_0402_1005Metric
- C34: value 1uF/50V -> 100nF/50V; footprint Capacitor_SMD:C_0603_1608Metric -> Capacitor_SMD:C_0402_1005Metric
- C36, C60: value 100nF/50V -> 47uF/50V; footprint Capacitor_SMD:C_0402_1005Metric -> Capacitor_SMD:CP_Elec_8x10.5
- C4: value 100nF -> 47uF; footprint Capacitor_SMD:C_0402_1005Metric -> Capacitor_SMD:C_0603_1608Metric
- C40, C64: value 100nF/50V -> 100nF
- C41: value 47uF/50V -> 1uF/50V; footprint Capacitor_SMD:CP_Elec_8x10.5 -> Capacitor_SMD:C_0603_1608Metric
- C42, C43, C66, C67: value 47uF/50V -> 100nF/50V; footprint Capacitor_SMD:CP_Elec_8x10.5 -> Capacitor_SMD:C_0402_1005Metric
- C45: value 22nF -> 100nF/50V
- C46: value 22nF -> 4.7uF; footprint Capacitor_SMD:C_0402_1005Metric -> Capacitor_SMD:C_0805_2012Metric
- C49: value 100nF -> 1uF/50V; footprint Capacitor_SMD:C_0402_1005Metric -> Capacitor_SMD:C_0603_1608Metric
- C51: value 4.7uF -> 100nF/50V; footprint Capacitor_SMD:C_0805_2012Metric -> Capacitor_SMD:C_0402_1005Metric
- C52: value 4.7uF -> 47uF/50V; footprint Capacitor_SMD:C_0805_2012Metric -> Capacitor_SMD:CP_Elec_8x10.5
- C58: value 1uF/50V -> 100nF/50V; footprint Capacitor_SMD:C_0805_2012Metric -> Capacitor_SMD:C_0402_1005Metric
- C68: value 100nF -> 47uF/50V; footprint Capacitor_SMD:C_0402_1005Metric -> Capacitor_SMD:CP_Elec_8x10.5
- C69: value 100nF -> 100nF/50V
- C7: value 1uF -> 100nF
- C9: value 10pF -> 1uF
- D3: value SMBJ26A -> SS56; footprint Diode_SMD:D_SMB -> Diode_SMD:D_SMA
- D4: value SS14 -> SMBJ26A; footprint Diode_SMD:D_SMA -> Diode_SMD:D_SMB
- D6: value SS56 -> SS14
- H1: value BOOT -> SPARE_GPIO
- H10: value SWDIO -> CAN_VCC; footprint TestPoint:TestPoint_Pad_D1.0mm -> TestPoint:TestPoint_Pad_D2.0mm
- H11: value SWCLK -> CAN_H
- H12: value CAN_VCC -> CAN_L; footprint TestPoint:TestPoint_Pad_D2.0mm -> TestPoint:TestPoint_Pad_D1.0mm
- H13: value CAN_H -> CAN_GND; footprint TestPoint:TestPoint_Pad_D1.0mm -> TestPoint:TestPoint_Pad_D2.0mm
- H14: value CAN_L -> SWDIO
- H15: value CAN_GND -> SWCLK; footprint TestPoint:TestPoint_Pad_D2.0mm -> TestPoint:TestPoint_Pad_D1.0mm
- H16: value SW -> CC2
- H17: value CC2 -> CC1; footprint TestPoint:TestPoint_Pad_D2.0mm -> TestPoint:TestPoint_Pad_D1.0mm
- H18: value CC1 -> SW; footprint TestPoint:TestPoint_Pad_D2.0mm -> TestPoint:TestPoint_Pad_D1.0mm
- H20: value +3V3 -> +24V
- H21: value +24V -> +3V3
- H25: value TMC3_DIAG -> TMC4_DIAG
- H26: value TMC1_INDEX -> TMC4_INDEX
- H27: value TMC2_INDEX -> TMC4_DIAG
- H28: value TMC3_INDEX -> TMC4_INDEX
- H3: value VDDA -> CAN_RX; footprint TestPoint:TestPoint_Pad_D2.0mm -> TestPoint:TestPoint_Pad_D1.0mm
- H30: value TMC5_DIAG -> TMC4_INDEX
- H31: value TMC6_DIAG -> TMC4_DIAG
- H33: value TMC5_INDEX -> TMC4_DIAG
- H34: value TMC6_INDEX -> TMC4_INDEX
- H4: value VREF+ -> CAN_TX; footprint TestPoint:TestPoint_Pad_D2.0mm -> TestPoint:TestPoint_Pad_D1.0mm
- H5: value SPARE_GPIO -> BOOT
- H6: value CAN_RX -> USART2
- H7: value USART2 -> USART1
- H8: value CAN_TX -> VDDA; footprint TestPoint:TestPoint_Pad_D1.0mm -> TestPoint:TestPoint_Pad_D2.0mm
- H9: value USART1 -> VREF+; footprint TestPoint:TestPoint_Pad_D1.0mm -> TestPoint:TestPoint_Pad_D2.0mm
- J1: value EXTN_PWR -> BTN1; footprint Connector_Molex:Molex_SPOX_5267-02A_1x02_P2.50mm_Vertical -> Connector:FanPinHeader_1x03_P2.54mm_Vertical
- J10: value STEP_MOTOR_5 -> STEP_MOTOR_2
- J11: value STEP_MOTOR_6 -> STEP_MOTOR_5
- J12: value BTN1 -> STEP_MOTOR_3; footprint Connector:FanPinHeader_1x03_P2.54mm_Vertical -> TerminalBlock_Phoenix:TerminalBlock_Phoenix_MKDS-1,5-4-5.08_1x04_P5.08mm_Horizontal
- J13: value FAN1 -> STEP_MOTOR_6; footprint Connector:FanPinHeader_1x03_P2.54mm_Vertical -> TerminalBlock_Phoenix:TerminalBlock_Phoenix_MKDS-1,5-4-5.08_1x04_P5.08mm_Horizontal
- J2: value PWR_BATT -> CAN SOCKET; footprint Connector_AMASS:AMASS_XT60PW-F_1x02_P7.20mm_Horizontal -> Connector_Molex:Molex_Pico-Lock_504050-0791_1x07-1MP_P1.50mm_Horizontal
- J3: value PWR_24V -> EXTN_PWR; footprint TerminalBlock:TerminalBlock_MaiXu_MX126-5.0-02P_1x02_P5.00mm -> Connector_Molex:Molex_SPOX_5267-02A_1x02_P2.50mm_Vertical
- J4: value CAN SOCKET -> FAN1; footprint Connector_Molex:Molex_Pico-Lock_504050-0791_1x07-1MP_P1.50mm_Horizontal -> Connector:FanPinHeader_1x03_P2.54mm_Vertical
- J6: value STEP_MOTOR_1 -> PWR_BATT; footprint TerminalBlock_Phoenix:TerminalBlock_Phoenix_MKDS-1,5-4-5.08_1x04_P5.08mm_Horizontal -> Connector_AMASS:AMASS_XT60PW-F_1x02_P7.20mm_Horizontal
- J7: value STEP_MOTOR_2 -> STEP_MOTOR_4
- J8: value STEP_MOTOR_3 -> STEP_MOTOR_1
- J9: value STEP_MOTOR_4 -> PWR_24V; footprint TerminalBlock_Phoenix:TerminalBlock_Phoenix_MKDS-1,5-4-5.08_1x04_P5.08mm_Horizontal -> TerminalBlock:TerminalBlock_MaiXu_MX126-5.0-02P_1x02_P5.00mm
- JP1: value TMC1_SPREAD -> CAN TERM; footprint Jumper:SolderJumper-3_P1.3mm_Bridged2Bar12_RoundedPad1.0x1.5mm -> Jumper:SolderJumper-2_P1.3mm_Open_RoundedPad1.0x1.5mm
- JP3: value TMC3_SPREAD -> TMC4_SPREAD
- JP5: value TMC5_SPREAD -> TMC4_SPREAD
- JP6: value TMC6_SPREAD -> TMC4_SPREAD
- JP7: value CAN TERM -> TMC4_SPREAD; footprint Jumper:SolderJumper-2_P1.3mm_Open_RoundedPad1.0x1.5mm -> Jumper:SolderJumper-3_P1.3mm_Bridged2Bar12_RoundedPad1.0x1.5mm
- R1: value 0R -> 10kR
- R10: value 100R -> 1.1kR
- R11: value 100R -> 1kR
- R12: value 20kR -> 390R
- R15: renamed from R30; value 0R11 -> 20kR; footprint Resistor_SMD:R_1206_3216Metric -> Resistor_SMD:R_0402_1005Metric
- R17: renamed from R36; value 20kR -> 0R11; footprint Resistor_SMD:R_0402_1005Metric -> Resistor_SMD:R_1206_3216Metric
- R18: value 0R11 -> 100R; footprint Resistor_SMD:R_1206_3216Metric -> Resistor_SMD:R_0402_1005Metric
- R19, R20, R34, R35: value 0R11 -> 20kR; footprint Resistor_SMD:R_1206_3216Metric -> Resistor_SMD:R_0402_1005Metric
- R2: value 10kR -> 0R
- R21, R22, R37: value 20kR -> 0R11; footprint Resistor_SMD:R_0402_1005Metric -> Resistor_SMD:R_1206_3216Metric
- R23, R28, R38: value 20kR -> 100R
- R25: value 100R -> 20kR
- R26: value 100R -> 0R11; footprint Resistor_SMD:R_0402_1005Metric -> Resistor_SMD:R_1206_3216Metric
- R39: value 120R -> 20kR
- R40: value 1.1kR -> 20kR
- R41: value 1kR -> 0R11; footprint Resistor_SMD:R_0402_1005Metric -> Resistor_SMD:R_1206_3216Metric
- R42: value 390R -> 0R11; footprint Resistor_SMD:R_0402_1005Metric -> Resistor_SMD:R_1206_3216Metric
- R5: value 33kR -> 5.1kR; footprint Resistor_SMD:R_0805_2012Metric -> Resistor_SMD:R_0402_1005Metric
- R6: value 10kR -> 5.1kR; footprint Resistor_SMD:R_0805_2012Metric -> Resistor_SMD:R_0402_1005Metric
- R7: value 5.1kR -> 33kR; footprint Resistor_SMD:R_0402_1005Metric -> Resistor_SMD:R_0805_2012Metric
- R8: value 5.1kR -> 10kR; footprint Resistor_SMD:R_0402_1005Metric -> Resistor_SMD:R_0805_2012Metric
- R9: value 100R -> 120R
- U10: value ISO1042DWVR -> TMC2209-LA-T; footprint lcsc:SOIC-8_L7.5-W5.9-P1.27-LS11.5-BL -> lcsc:QFN-28_L5.0-W5.0-P0.50-BL-EP
- U2: value NCP1117-3.3_SOT223 -> XL4005E1; footprint Package_TO_SOT_SMD:SOT-223-3_TabPin2 -> lcsc:TO-263-5_L10.2-W9.2-P1.70-TL
- U3: value XL4005E1 -> NCP1117-3.3_SOT223; footprint lcsc:TO-263-5_L10.2-W9.2-P1.70-TL -> Package_TO_SOT_SMD:SOT-223-3_TabPin2
- U4: value TMC2209-LA-T -> ISO1042DWVR; footprint lcsc:QFN-28_L5.0-W5.0-P0.50-BL-EP -> lcsc:SOIC-8_L7.5-W5.9-P1.27-LS11.5-BL
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- renumbered C59 to C27, H29 to H23, H32 to H24, JP4 to JP2, R24 to R13, R27 to R14, R33 to R16, U7 to U5
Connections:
- net TMC3_SPREAD renamed Net-(JP3-C)
- net TMC4_SPREAD renamed Net-(JP2-C)
- net TMC5_SPREAD renamed Net-(JP5-C)
- net TMC6_SPREAD renamed Net-(JP6-C)
- C10 pad 1: OSC_IN -> VREF+
- C10 pad 2: GND -> Net-(C10-Pad2)
- C13 pad 1: VBUS -> +24V
- C16 pad 1: +24V -> Net-(D5-A)
- C17 pad 1: Net-(D4-A) -> Net-(D5-A)
- C17 pad 2: GND -> Net-(U2-FB)
- C18 pad 1: Net-(D4-A) -> VBUS
- C19 pad 1: Net-(D4-A) -> Net-(D6-A)
- C19 pad 2: Net-(U3-FB) -> GND
- C2 pad 1: Net-(C2-Pad1) -> GND
- C2 pad 2: Net-(C2-Pad2) -> OSC_OUT
- C20 pad 1: Net-(U4-CPI) -> +3V3
- C20 pad 2: Net-(U4-CPO) -> GND
- C21 pad 1: Net-(U5-CPI) -> CAN_VCC
- C21 pad 2: Net-(U5-CPO) -> CAN_GND
- C22 pad 1: Net-(U7-CPI) -> GND
- C22 pad 2: Net-(U7-CPO) -> Net-(U5-5VOUT)
- C23 pad 1: +24V -> Net-(U5-CPI)
- C23 pad 2: Net-(U7-VCP) -> Net-(U5-CPO)
- C24 pad 1: GND -> +24V
- C24 pad 2: Net-(U7-5VOUT) -> Net-(U5-VCP)
- C25 pad 1: +3V3 -> +24V
- C29 pad 1: +24V -> +3V3
- C3 pad 1: Net-(C2-Pad1) -> OSC_IN
- C3 pad 2: Net-(C2-Pad2) -> GND
- C30 pad 1: +3V3 -> GND
- C30 pad 2: GND -> Net-(U6-5VOUT)
- C31 pad 1: +3V3 -> Net-(U6-CPI)
- C31 pad 2: GND -> Net-(U6-CPO)
- C32 pad 2: GND -> Net-(U6-VCP)
- C37 pad 1: +24V -> +3V3
- C38 pad 1: +24V -> GND
- C38 pad 2: GND -> Net-(U7-5VOUT)
- C39 pad 1: +24V -> Net-(U7-CPI)
- C39 pad 2: GND -> Net-(U7-CPO)
- C4 pad 1: Net-(C2-Pad1) -> Net-(C4-Pad1)
- C4 pad 2: Net-(C2-Pad2) -> Net-(C10-Pad2)
- C40 pad 2: GND -> Net-(U7-VCP)
- C45 pad 1: Net-(U8-CPI) -> +3V3
- C45 pad 2: Net-(U8-CPO) -> GND
- C46 pad 1: Net-(U9-CPI) -> GND
- C46 pad 2: Net-(U9-CPO) -> Net-(U8-5VOUT)
- C49 pad 2: Net-(U9-VCP) -> GND
- C5 pad 1: Net-(C2-Pad1) -> Net-(C4-Pad1)
- C5 pad 2: Net-(C2-Pad2) -> Net-(C10-Pad2)
- C51 pad 1: GND -> +24V
- C51 pad 2: Net-(U8-5VOUT) -> GND
- C52 pad 1: GND -> +24V
- C52 pad 2: Net-(U9-5VOUT) -> GND
- C54 pad 1: +3V3 -> GND
- C54 pad 2: GND -> Net-(U9-5VOUT)
- C55 pad 1: +3V3 -> Net-(U9-CPI)
- C55 pad 2: GND -> Net-(U9-CPO)
- C6 pad 1: VDD33A -> Net-(C4-Pad1)
- C6 pad 2: Net-(C2-Pad2) -> Net-(C10-Pad2)
- C61 pad 1: +24V -> +3V3
- C63 pad 1: +24V -> Net-(U10-CPI)
- C63 pad 2: GND -> Net-(U10-CPO)
- C64 pad 2: GND -> Net-(U10-VCP)
- C66 pad 2: unconnected-(C66-Pad2) -> GND
- C68 pad 1: +3V3 -> +24V
- C69 pad 1: CAN_VCC -> +3V3
- C69 pad 2: CAN_GND -> GND
- C7 pad 1: Net-(C7-Pad1) -> Net-(C4-Pad1)
- C7 pad 2: Net-(C2-Pad2) -> Net-(C10-Pad2)
- C8 pad 1: VREF+ -> VDD33A
- C8 pad 2: Net-(C2-Pad2) -> Net-(C10-Pad2)
- C9 pad 1: GND -> Net-(C9-Pad1)
- C9 pad 2: OSC_OUT -> Net-(C10-Pad2)
- D1 pad 1: Net-(D1-K) -> BIDIR_24V
- D2 pad 1: Net-(D1-K) -> BIDIR_24V
- D3 pad 1: +24V -> Net-(D3-K)
- D4 pad 1: +3.3V -> +24V
- D4 pad 2: Net-(D4-A) -> GND
- D6 pad 1: Net-(D6-K) -> +3.3V
- D6 pad 2: GND -> Net-(D6-A)
- F1 pad 1: Net-(D1-K) -> BIDIR_24V
- FB1 pad 2: Net-(C2-Pad1) -> Net-(C4-Pad1)
- FB2 pad 1: Net-(C2-Pad1) -> Net-(C4-Pad1)
- FB2 pad 2: Net-(C7-Pad1) -> Net-(C9-Pad1)
- H1 pad 1: CAN_RX -> Net-(U1-PA2)
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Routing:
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- added copper zone on F.Cu, net BIDIR_24V
- added copper zone on F.Cu, net Net-(U10-5VOUT)
- added copper zone on F.Cu, net Net-(U5-5VOUT)
- added copper zone on F.Cu, net Net-(U6-5VOUT)
- added copper zone on F.Cu, net Net-(U8-5VOUT)
- added copper zone on F.Cu, net Net-(U9-5VOUT)
- added copper zone on F.Cu, net TMC1_A1
- added copper zone on F.Cu, net TMC1_A2
- added copper zone on F.Cu, net TMC1_B1
- added copper zone on F.Cu, net TMC1_B2
- added copper zone on F.Cu, net TMC2_A1
- added copper zone on F.Cu, net TMC2_A2
- added copper zone on F.Cu, net TMC2_B1
- added copper zone on F.Cu, net TMC2_B2
- added copper zone on F.Cu, net TMC6_A1
- added copper zone on F.Cu, net TMC6_A2
- added copper zone on F.Cu, net TMC6_B1
- added copper zone on F.Cu, net TMC6_B2
- removed copper zone on F.Cu, net TMC4_A1
- removed copper zone on F.Cu, net TMC4_A2
- removed copper zone on F.Cu, net TMC4_B1
- removed copper zone on F.Cu, net TMC4_B2
